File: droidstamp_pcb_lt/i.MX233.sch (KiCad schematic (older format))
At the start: 90 parts, among them IC1 iMX233, J1 MICROSD, P1 CONN_12X2, P10 CONN_1, P2 CONN_12X2, P3 CONN_1, P5 CONN_1, P6 CONN_5X2, P7 CONN_1, Q1 MMDT3904, U1 ADM3101E, U3 M25P32, X1 24MHz

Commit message: reconnect
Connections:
- wire segments 400 -> 401

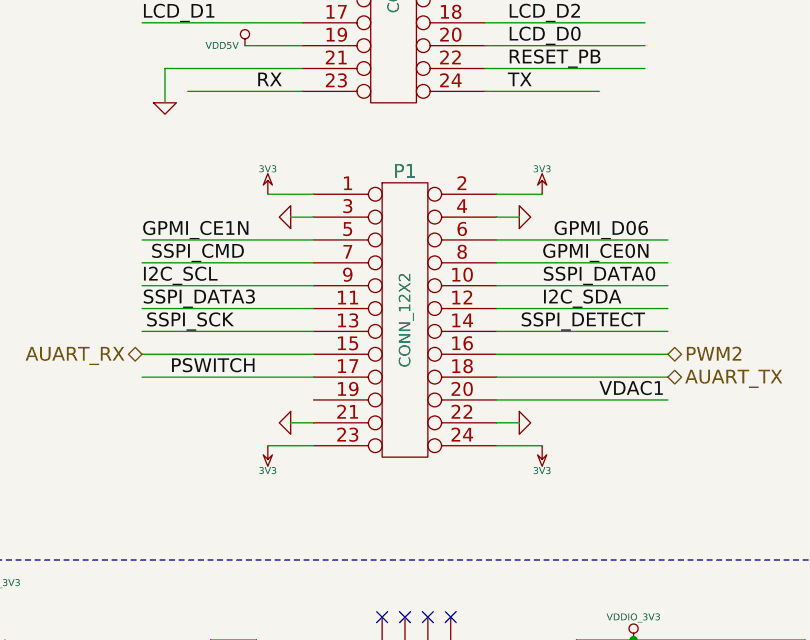
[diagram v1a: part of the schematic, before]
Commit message: USB PC compatible connector
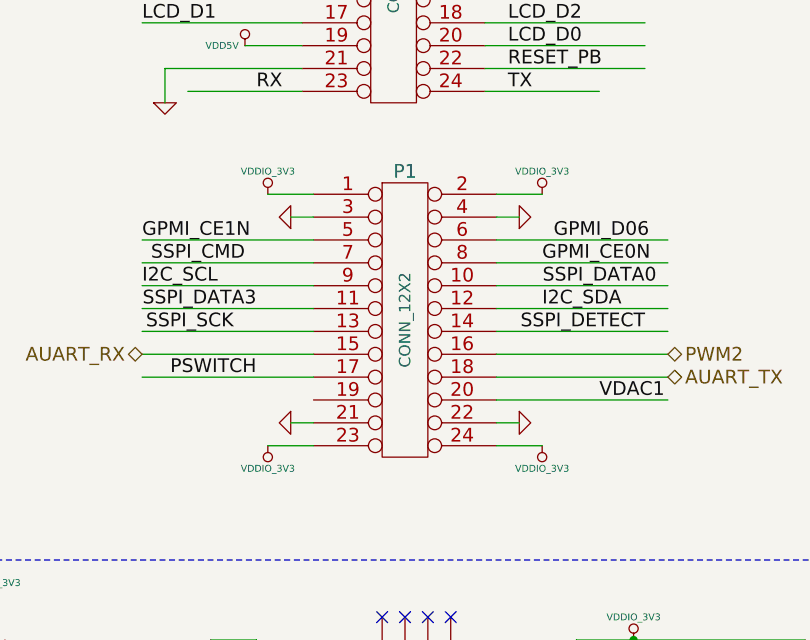
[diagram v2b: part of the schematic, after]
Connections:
- net labels removed: 3V3

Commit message: ratnets revision
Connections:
- wire segments 401 -> 396
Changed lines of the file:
@@
-EESchema Schematic File Version 2  date Mon 18 Jun 2012 02:03:20 AM COT
+EESchema Schematic File Version 2  date Mon 18 Jun 2012 06:53:05 AM COT
 LIBS:con-jack
 LIBS:zxct1009
@@
 $Descr A3 16535 11700
 encoding utf-8
-Sheet 2 4
+Sheet 4 4
 Title ""
 Date "18 jun 2012"
@@
 Text Label 13250 5200 2    60   ~ 0
 SSPI_SCK
-Text Label 15100 5000 2    60   ~ 0
+Text Label 15050 5000 2    60   ~ 0
 SSPI_DATA0
 Text Label 13350 5100 2    60   ~ 0
@@
 Text HLabel 15150 5300 2    60   BiDi ~ 0
 PWM2
-Text Label 9050 4350 2    60   ~ 0
-SSPI_DATA3
-Text HLabel 9250 4050 2    60   BiDi ~ 0
-GPMI_CE0N
-Text HLabel 9250 4500 2    60   BiDi ~ 0
-SSPI_DETECT
-Text HLabel 9250 3950 2    60   BiDi ~ 0
-GPMI_CE1N
-Text HLabel 9250 3850 2    60   BiDi ~ 0
-GPMI_D06
-Text HLabel 9250 4350 2    60   BiDi ~ 0
-SSPI_DATA3
-Text Label 15050 5200 2    60   ~ 0
+Text Label 15100 5200 2    60   ~ 0
 SSPI_DETECT
 Text Label 12850 5000 0    60   ~ 0
 I2C_SCL
-Text Label 14600 5100 0    60   ~ 0
+Text Label 14550 5100 0    60   ~ 0
 I2C_SDA
 Text Label 12850 4800 0    60   ~ 0
 GPMI_CE1N
-Text Label 14600 4900 0    60   ~ 0
+Text Label 14550 4900 0    60   ~ 0
 GPMI_CE0N
-Text Label 8550 3850 0    60   ~ 0
-GPMI_D06
 Text Label 14650 4800 0    60   ~ 0
 GPMI_D06
@@
 	0    1    -1   0
 $EndComp
+$Comp
+L GND #PWR085
+U 1 1 4FDE97DD
+P 14500 5600
+F 0 "#PWR085" H 14500 5600 30  0001 C CNN
+F 1 "GND" H 14500 5530 30  0001 C CNN
+	1    14500 5600
+	0    -1   1    0
+$EndComp
+$Comp
+L GND #PWR086
+U 1 1 4FDE97EB
+P 13500 5600
+F 0 "#PWR086" H 13500 5600 30  0001 C CNN
+F 1 "GND" H 13500 5530 30  0001 C CNN
+	1    13500 5600
+	0    1    1    0
+$EndComp
+$Comp
+L VDDIO_3V3 #PWR087
+U 1 1 4FDE976D
+P 13400 4600
+F 0 "#PWR087" H 13400 4700 30  0001 C CNN
+F 1 "VDDIO_3V3" H 13400 4700 30  0000 C CNN
+	1    13400 4600
+	1    0    0    -1
+$EndComp
+$Comp
+L VDDIO_3V3 #PWR088
+U 1 1 4FDE9773
+P 14600 4600
+F 0 "#PWR088" H 14600 4700 30  0001 C CNN
+F 1 "VDDIO_3V3" H 14600 4700 30  0000 C CNN
+	1    14600 4600
+	1    0    0    -1
+$EndComp
+$Comp
+L VDDIO_3V3 #PWR089
+U 1 1 4FDE9779
+P 13400 5700
+F 0 "#PWR089" H 13400 5800 30  0001 C CNN
+F 1 "VDDIO_3V3" H 13400 5800 30  0000 C CNN
+	1    13400 5700
+	1    0    0    1
+$EndComp
+$Comp
+L VDDIO_3V3 #PWR090
+U 1 1 4FDE977F
+P 14600 5700
+F 0 "#PWR090" H 14600 5800 30  0001 C CNN
+F 1 "VDDIO_3V3" H 14600 5800 30  0000 C CNN
+	1    14600 5700
+	1    0    0    1
+$EndComp
 Wire Notes Line
 	8400 6300 8400 9250
@@
 	9500 5100 10250 5100
 Wire Wire Line
-	9650 5000 10250 5000
+	9500 5000 10250 5000
 Wire Wire Line
 	9500 4900 10250 4900
@@
 	11800 5100 11050 5100
 Wire Wire Line
-	11650 5000 11050 5000
+	11050 5000 11800 5000
 Wire Wire Line
 	11800 4900 11050 4900
@@
 	11800 5200 11050 5200
 Wire Wire Line
-	9250 4500 8550 4500
-Wire Wire Line
-	9250 3850 8550 3850
-Wire Wire Line
-	8550 3950 9250 3950
-Wire Wire Line
-	9250 4050 8550 4050
-Wire Wire Line
-	8550 4350 9250 4350
-Wire Wire Line
 	15150 5300 14400 5300
 Wire Wire Line
@@
 Wire Wire Line
 	13600 5000 12850 5000
-$Comp
-L GND #PWR085
-U 1 1 4FDE97DD
-P 14500 5600
-F 0 "#PWR085" H 14500 5600 30  0001 C CNN
-F 1 "GND" H 14500 5530 30  0001 C CNN
-	1    14500 5600
-	0    -1   1    0
-$EndComp
 Wire Wire Line
 	14400 5700 14600 5700
 Wire Wire Line
 	14500 5600 14400 5600
-$Comp
-L GND #PWR086
-U 1 1 4FDE97EB
-P 13500 5600
-F 0 "#PWR086" H 13500 5600 30  0001 C CNN
-F 1 "GND" H 13500 5530 30  0001 C CNN
-	1    13500 5600
-	0    1    1    0
-$EndComp
 Wire Wire Line
 	13600 5700 13400 5700
 Wire Wire Line
 	13500 5600 13600 5600
-$Comp
-L VDDIO_3V3 #PWR087
-U 1 1 4FDE976D
-P 13400 4600
-F 0 "#PWR087" H 13400 4700 30  0001 C CNN
-F 1 "VDDIO_3V3" H 13400 4700 30  0000 C CNN
-	1    13400 4600
-	1    0    0    -1
-$EndComp
-$Comp
-L VDDIO_3V3 #PWR088
-U 1 1 4FDE9773
-P 14600 4600
-F 0 "#PWR088" H 14600 4700 30  0001 C CNN
-F 1 "VDDIO_3V3" H 14600 4700 30  0000 C CNN
-	1    14600 4600
-	1    0    0    -1
-$EndComp
-$Comp
-L VDDIO_3V3 #PWR089
-U 1 1 4FDE9779
-P 13400 5700
-F 0 "#PWR089" H 13400 5800 30  0001 C CNN
-F 1 "VDDIO_3V3" H 13400 5800 30  0000 C CNN
-	1    13400 5700
-	1    0    0    1
-$EndComp
-$Comp
-L VDDIO_3V3 #PWR090
-U 1 1 4FDE977F
-P 14600 5700
-F 0 "#PWR090" H 14600 5800 30  0001 C CNN
-F 1 "VDDIO_3V3" H 14600 5800 30  0000 C CNN
-	1    14600 5700
-	1    0    0    1
-$EndComp
 $EndSCHEMATC
